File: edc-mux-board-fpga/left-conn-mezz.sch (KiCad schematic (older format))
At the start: 86 parts, among them J13 Device 0, J14 Device 3, J15 Device 1, J16 Device 4, J17 Left Mezzanine Board Connecto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, J18 Left Mezzanine Board Connecto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, J19 Device 2, J20 Device 5

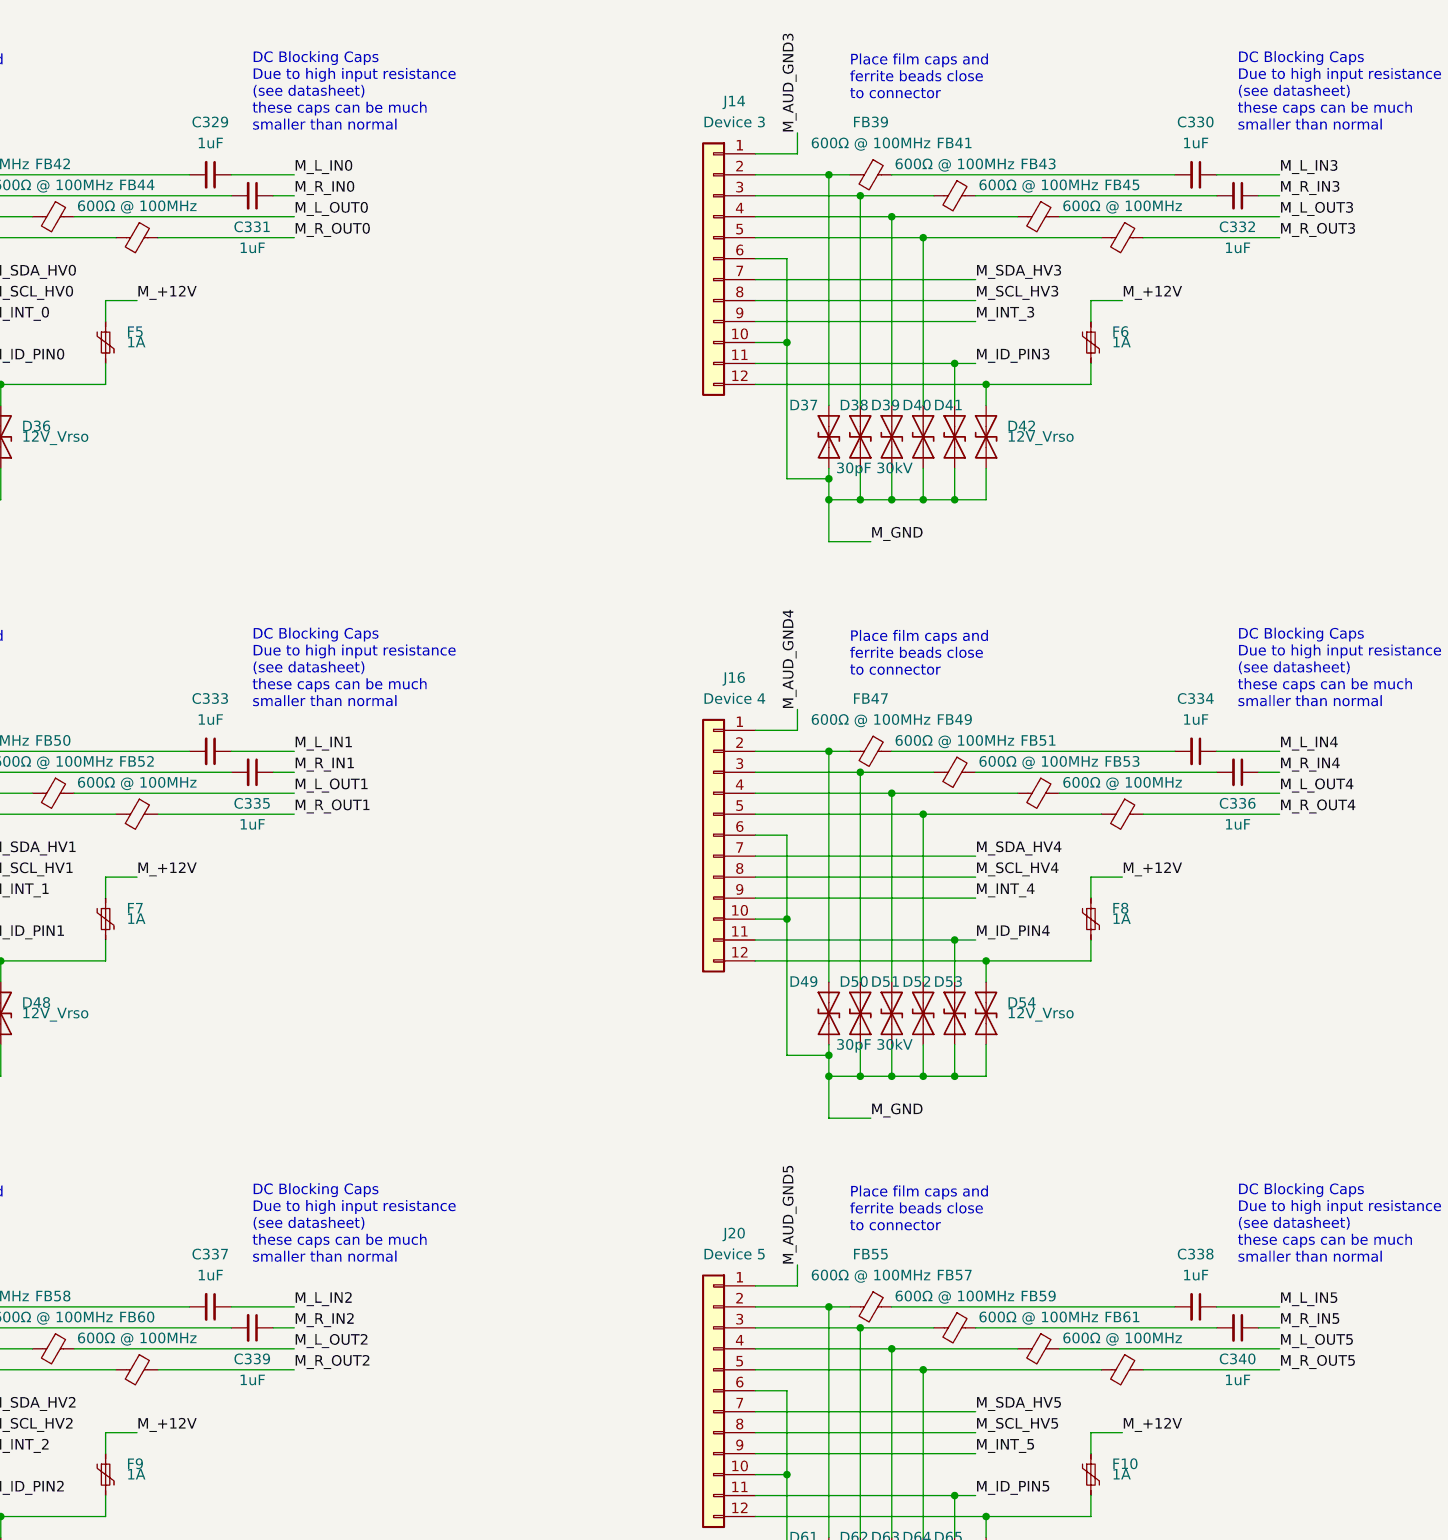
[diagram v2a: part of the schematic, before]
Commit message: assigned more footprints
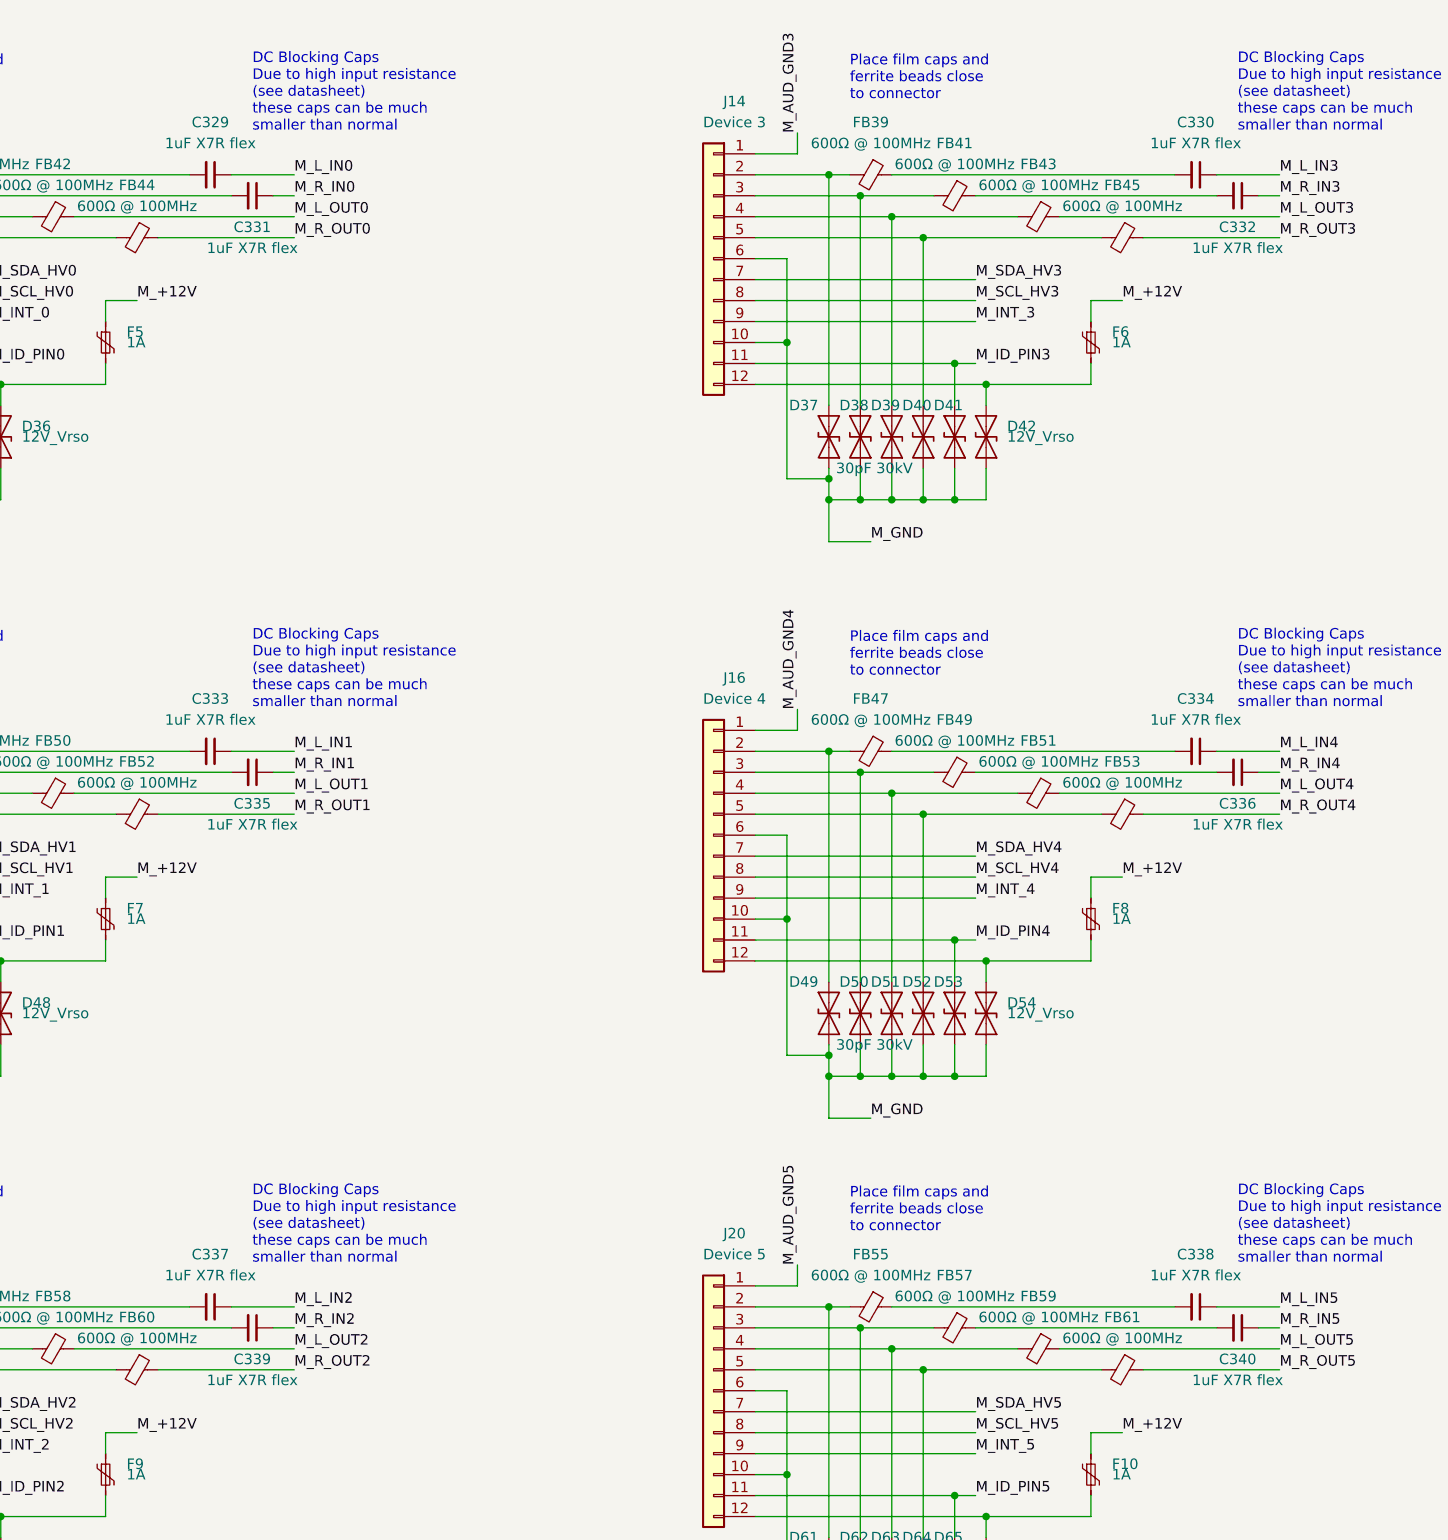
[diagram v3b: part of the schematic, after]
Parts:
- C329, C330, C331, C332, C333, C334, C335, C336, C337, C338, C339, C340: value 1uF -> 1uF X7R flex
- J13, J14, J15, J16, J19, J20: footprint Connector_PinHeader_1.27mm:PinHeader_2x06_P1.27mm_Vertical -> SW-TEConn:T4141012121-000; Manufacturer (none) -> TE Connectivity; Manufacturers Part Number (none) -> T4141012121-000
- J17: footprint (none) -> Connector_PinSocket_2.54mm:PinSocket_2x10_P2.54mm_Horizontal
- J18: footprint (none) -> Connector_PinHeader_2.54mm:PinHeader_2x10_P2.54mm_Vertical
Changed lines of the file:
@@
 F 0 "J13" H 650 2550 50  0000 C CNN
 F 1 "Device 0" H 650 2450 50  0000 C CNN
-F 2 "Connector_PinHeader_1.27mm:PinHeader_2x06_P1.27mm_Vertical" H 750 1800 50  0001 C CNN
-F 3 "~" H 750 1800 50  0001 C CNN
+F 2 "SW-TEConn:T4141012121-000" H 750 1800 50  0001 C CNN
+F 3 "https://www.te.com/commerce/DocumentDelivery/DDEController?Action=showdoc&DocId=Customer+Drawing%7FT4141012081000%7FA1%7Fpdf%7FEnglish%7FENG_CD_T4141012081000_A1.pdf%7FT4141012121-000" H 750 1800 50  0001 C CNN
+F 4 "TE Connectivity" H 0   0   50  0001 C CNN "Manufacturer"
+F 5 "T4141012121-000" H 0   0   50  0001 C CNN "Manufacturers Part Number"
 	1    750  1800
 	-1   0    0    -1
@@
 AR Path="/5CBF625C/5CC29ACF" Ref="C331"  Part="1"
 F 0 "C331" V 3400 1500 50  0000 C CNN
-F 1 "1uF" V 3500 1500 50  0000 C CNN
+F 1 "1uF X7R flex" V 3500 1500 50  0000 C CNN
 F 2 "Capacitor_SMD:C_0805_2012Metric" H 3250 1500 50  0001 C CNN
 F 3 "~" H 3250 1500 50  0001 C CNN
@@
 AR Path="/5CBF625C/5CC29AEF" Ref="C329"  Part="1"
 F 0 "C329" V 2800 1400 50  0000 C CNN
-F 1 "1uF" V 2900 1400 50  0000 C CNN
+F 1 "1uF X7R flex" V 2900 1400 50  0000 C CNN
 F 2 "Capacitor_SMD:C_0805_2012Metric" H 3050 1400 50  0001 C CNN
 F 3 "~" H 3050 1400 50  0001 C CNN
@@
 F 0 "J17" H 10400 6950 50  0000 C CNN
 F 1 "Left Mezzanine Board Connector (Daughterboard)" H 10400 2850 50  0000 C CNN
-F 2 "" H 10350 4950 50  0001 C CNN
+F 2 "Connector_PinSocket_2.54mm:PinSocket_2x10_P2.54mm_Horizontal" H 10350 4950 50  0001 C CNN
 F 3 "~" H 10350 4950 50  0001 C CNN
 	1    10350 4950
@@
 F 0 "J15" H 650 5300 50  0000 C CNN
 F 1 "Device 1" H 650 5200 50  0000 C CNN
-F 2 "Connector_PinHeader_1.27mm:PinHeader_2x06_P1.27mm_Vertical" H 750 4550 50  0001 C CNN
-F 3 "~" H 750 4550 50  0001 C CNN
+F 2 "SW-TEConn:T4141012121-000" H 750 4550 50  0001 C CNN
+F 3 "https://www.te.com/commerce/DocumentDelivery/DDEController?Action=showdoc&DocId=Customer+Drawing%7FT4141012081000%7FA1%7Fpdf%7FEnglish%7FENG_CD_T4141012081000_A1.pdf%7FT4141012121-000" H 750 4550 50  0001 C CNN
+F 4 "TE Connectivity" H 0   0   50  0001 C CNN "Manufacturer"
+F 5 "T4141012121-000" H 0   0   50  0001 C CNN "Manufacturers Part Number"
 	1    750  4550
 	-1   0    0    -1
@@
 AR Path="/5CBF625C/5D2B615F" Ref="C335"  Part="1"
 F 0 "C335" V 3400 4250 50  0000 C CNN
-F 1 "1uF" V 3500 4250 50  0000 C CNN
+F 1 "1uF X7R flex" V 3500 4250 50  0000 C CNN
 F 2 "Capacitor_SMD:C_0805_2012Metric" H 3250 4250 50  0001 C CNN
 F 3 "~" H 3250 4250 50  0001 C CNN
@@
 AR Path="/5CBF625C/5D2B6170" Ref="C333"  Part="1"
 F 0 "C333" V 2800 4150 50  0000 C CNN
-F 1 "1uF" V 2900 4150 50  0000 C CNN
+F 1 "1uF X7R flex" V 2900 4150 50  0000 C CNN
 F 2 "Capacitor_SMD:C_0805_2012Metric" H 3050 4150 50  0001 C CNN
 F 3 "~" H 3050 4150 50  0001 C CNN
@@
 F 0 "J19" H 650 7950 50  0000 C CNN
 F 1 "Device 2" H 650 7850 50  0000 C CNN
-F 2 "Connector_PinHeader_1.27mm:PinHeader_2x06_P1.27mm_Vertical" H 750 7200 50  0001 C CNN
-F 3 "~" H 750 7200 50  0001 C CNN
+F 2 "SW-TEConn:T4141012121-000" H 750 7200 50  0001 C CNN
+F 3 "https://www.te.com/commerce/DocumentDelivery/DDEController?Action=showdoc&DocId=Customer+Drawing%7FT4141012081000%7FA1%7Fpdf%7FEnglish%7FENG_CD_T4141012081000_A1.pdf%7FT4141012121-000" H 750 7200 50  0001 C CNN
+F 4 "TE Connectivity" H 0   0   50  0001 C CNN "Manufacturer"
+F 5 "T4141012121-000" H 0   0   50  0001 C CNN "Manufacturers Part Number"
 	1    750  7200
 	-1   0    0    -1
@@
 AR Path="/5CBF625C/5D2CED34" Ref="C339"  Part="1"
 F 0 "C339" V 3400 6900 50  0000 C CNN
-F 1 "1uF" V 3500 6900 50  0000 C CNN
+F 1 "1uF X7R flex" V 3500 6900 50  0000 C CNN
 F 2 "Capacitor_SMD:C_0805_2012Metric" H 3250 6900 50  0001 C CNN
 F 3 "~" H 3250 6900 50  0001 C CNN
@@
 AR Path="/5CBF625C/5D2CED45" Ref="C337"  Part="1"
 F 0 "C337" V 2800 6800 50  0000 C CNN
-F 1 "1uF" V 2900 6800 50  0000 C CNN
+F 1 "1uF X7R flex" V 2900 6800 50  0000 C CNN
 F 2 "Capacitor_SMD:C_0805_2012Metric" H 3050 6800 50  0001 C CNN
 F 3 "~" H 3050 6800 50  0001 C CNN
@@
 F 0 "J14" H 5350 2550 50  0000 C CNN
 F 1 "Device 3" H 5350 2450 50  0000 C CNN
-F 2 "Connector_PinHeader_1.27mm:PinHeader_2x06_P1.27mm_Vertical" H 5450 1800 50  0001 C CNN
-F 3 "~" H 5450 1800 50  0001 C CNN
+F 2 "SW-TEConn:T4141012121-000" H 5450 1800 50  0001 C CNN
+F 3 "https://www.te.com/commerce/DocumentDelivery/DDEController?Action=showdoc&DocId=Customer+Drawing%7FT4141012081000%7FA1%7Fpdf%7FEnglish%7FENG_CD_T4141012081000_A1.pdf%7FT4141012121-000" H 5450 1800 50  0001 C CNN
+F 4 "TE Connectivity" H 0   0   50  0001 C CNN "Manufacturer"
+F 5 "T4141012121-000" H 0   0   50  0001 C CNN "Manufacturers Part Number"
 	1    5450 1800
 	-1   0    0    -1
@@
 AR Path="/5CBF625C/5D2E2286" Ref="C332"  Part="1"
 F 0 "C332" V 8100 1500 50  0000 C CNN
-F 1 "1uF" V 8200 1500 50  0000 C CNN
+F 1 "1uF X7R flex" V 8200 1500 50  0000 C CNN
 F 2 "Capacitor_SMD:C_0805_2012Metric" H 7950 1500 50  0001 C CNN
 F 3 "~" H 7950 1500 50  0001 C CNN
@@
 AR Path="/5CBF625C/5D2E2297" Ref="C330"  Part="1"
 F 0 "C330" V 7500 1400 50  0000 C CNN
-F 1 "1uF" V 7600 1400 50  0000 C CNN
+F 1 "1uF X7R flex" V 7600 1400 50  0000 C CNN
 F 2 "Capacitor_SMD:C_0805_2012Metric" H 7750 1400 50  0001 C CNN
 F 3 "~" H 7750 1400 50  0001 C CNN
@@
 F 0 "J16" H 5350 5300 50  0000 C CNN
 F 1 "Device 4" H 5350 5200 50  0000 C CNN
-F 2 "Connector_PinHeader_1.27mm:PinHeader_2x06_P1.27mm_Vertical" H 5450 4550 50  0001 C CNN
-F 3 "~" H 5450 4550 50  0001 C CNN
+F 2 "SW-TEConn:T4141012121-000" H 5450 4550 50  0001 C CNN
+F 3 "https://www.te.com/commerce/DocumentDelivery/DDEController?Action=showdoc&DocId=Customer+Drawing%7FT4141012081000%7FA1%7Fpdf%7FEnglish%7FENG_CD_T4141012081000_A1.pdf%7FT4141012121-000" H 5450 4550 50  0001 C CNN
+F 4 "TE Connectivity" H 0   0   50  0001 C CNN "Manufacturer"
+F 5 "T4141012121-000" H 0   0   50  0001 C CNN "Manufacturers Part Number"
 	1    5450 4550
 	-1   0    0    -1
@@
 AR Path="/5CBF625C/5D2FA18F" Ref="C336"  Part="1"
 F 0 "C336" V 8100 4250 50  0000 C CNN
-F 1 "1uF" V 8200 4250 50  0000 C CNN
+F 1 "1uF X7R flex" V 8200 4250 50  0000 C CNN
 F 2 "Capacitor_SMD:C_0805_2012Metric" H 7950 4250 50  0001 C CNN
 F 3 "~" H 7950 4250 50  0001 C CNN
@@
 AR Path="/5CBF625C/5D2FA1A0" Ref="C334"  Part="1"
 F 0 "C334" V 7500 4150 50  0000 C CNN
-F 1 "1uF" V 7600 4150 50  0000 C CNN
+F 1 "1uF X7R flex" V 7600 4150 50  0000 C CNN
 F 2 "Capacitor_SMD:C_0805_2012Metric" H 7750 4150 50  0001 C CNN
 F 3 "~" H 7750 4150 50  0001 C CNN
@@
 F 0 "J20" H 5350 7950 50  0000 C CNN
 F 1 "Device 5" H 5350 7850 50  0000 C CNN
-F 2 "Connector_PinHeader_1.27mm:PinHeader_2x06_P1.27mm_Vertical" H 5450 7200 50  0001 C CNN
-F 3 "~" H 5450 7200 50  0001 C CNN
+F 2 "SW-TEConn:T4141012121-000" H 5450 7200 50  0001 C CNN
+F 3 "https://www.te.com/commerce/DocumentDelivery/DDEController?Action=showdoc&DocId=Customer+Drawing%7FT4141012081000%7FA1%7Fpdf%7FEnglish%7FENG_CD_T4141012081000_A1.pdf%7FT4141012121-000" H 5450 7200 50  0001 C CNN
+F 4 "TE Connectivity" H 0   0   50  0001 C CNN "Manufacturer"
+F 5 "T4141012121-000" H 0   0   50  0001 C CNN "Manufacturers Part Number"
 	1    5450 7200
 	-1   0    0    -1
@@
 AR Path="/5CBF625C/5D310EC6" Ref="C340"  Part="1"
 F 0 "C340" V 8100 6900 50  0000 C CNN
-F 1 "1uF" V 8200 6900 50  0000 C CNN
+F 1 "1uF X7R flex" V 8200 6900 50  0000 C CNN
 F 2 "Capacitor_SMD:C_0805_2012Metric" H 7950 6900 50  0001 C CNN
 F 3 "~" H 7950 6900 50  0001 C CNN
@@
 AR Path="/5CBF625C/5D310ED7" Ref="C338"  Part="1"
 F 0 "C338" V 7500 6800 50  0000 C CNN
-F 1 "1uF" V 7600 6800 50  0000 C CNN
+F 1 "1uF X7R flex" V 7600 6800 50  0000 C CNN
 F 2 "Capacitor_SMD:C_0805_2012Metric" H 7750 6800 50  0001 C CNN
 F 3 "~" H 7750 6800 50  0001 C CNN
@@
 F 0 "J18" H 13950 6950 50  0000 C CNN
 F 1 "Left Mezzanine Board Connector (Motherboard)" H 13950 2850 50  0000 C CNN
-F 2 "" H 13900 4950 50  0001 C CNN
+F 2 "Connector_PinHeader_2.54mm:PinHeader_2x10_P2.54mm_Vertical" H 13900 4950 50  0001 C CNN
 F 3 "~" H 13900 4950 50  0001 C CNN
 	1    13900 4950
